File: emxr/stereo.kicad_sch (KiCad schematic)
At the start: 56 parts, among them IC401 NJM2068DD, IC402 NJM4580, IC403 NJM2068DD, IC404 NJM4580

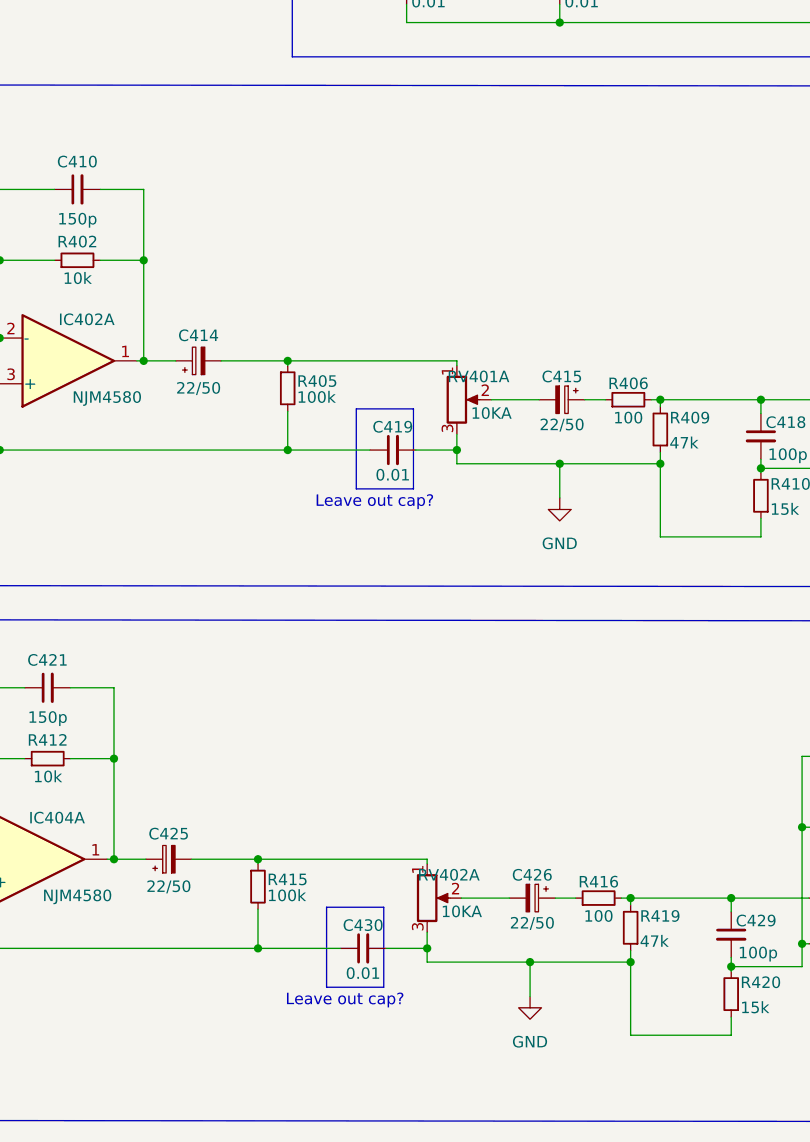
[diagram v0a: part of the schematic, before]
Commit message: finish footprints, starting on component placement
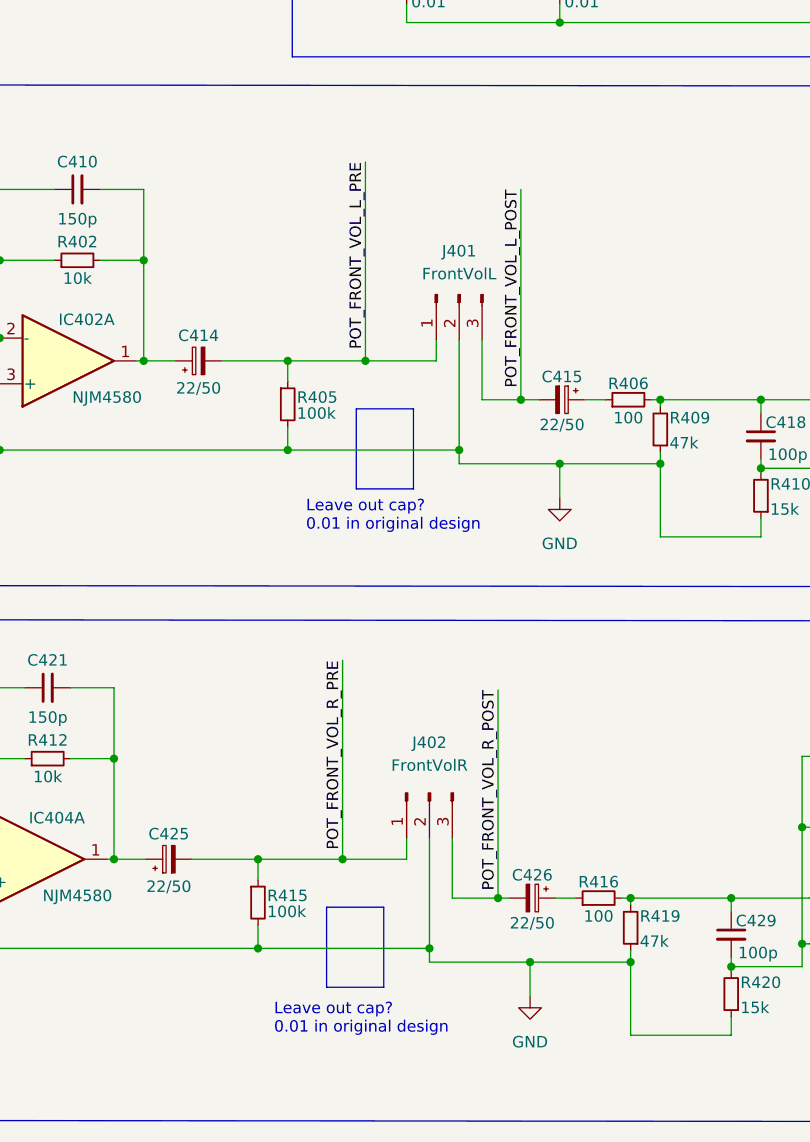
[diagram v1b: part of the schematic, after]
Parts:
- removed C419, C430: 0.01, symbol Device:C_Small
- removed RV401, RV402: 10KA, symbol Device:R_Potentiometer_Dual_Separate
- added J401: FrontVolL, Connector_JST:JST_XH_B3B-XH-A_1x03_P2.50mm_Vertical, symbol Connector:Conn_01x03_Male
- added J402: FrontVolR, Connector_JST:JST_XH_B3B-XH-A_1x03_P2.50mm_Vertical, symbol Connector:Conn_01x03_Male
- C401, C402, C403, C404, C405, C406, C407, C408, C409, C420: footprint (none) -> Capacitor_THT:C_Disc_D3.8mm_W2.6mm_P2.50mm
- C410, C411, C416, C418, C421, C422, C427: footprint (none) -> Capacitor_THT:C_Disc_D5.0mm_W2.5mm_P2.50mm
- C412, C423: footprint (none) -> Capacitor_THT:CP_Radial_D10.0mm_P5.00mm
- C413, C414, C415, C424, C425, C426: footprint (none) -> Capacitor_THT:CP_Radial_D5.0mm_P2.00mm
- C417, C428: footprint (none) -> Capacitor_THT:CP_Radial_D6.3mm_P2.50mm
- C429: footprint (none) -> Capacitor_THT:C_Disc_D5.1mm_W3.2mm_P5.00mm
- IC401, IC402, IC403, IC404: footprint (none) -> Package_DIP:DIP-8_W7.62mm_Socket_LongPads
- R401, R402, R403, R404, R405, R406, R407, R408, R409, R410, R411, R412, R413, R414, R415, R416, R417, R418, R419, R420: footprint (none) -> Resistor_THT:R_Axial_DIN0207_L6.3mm_D2.5mm_P10.16mm_Horizontal
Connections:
- net GND: now also J401.2 (Pin_2), J402.2 (Pin_2)
- net POT_FRONT_VOL_L_PRE: now reaches C414.2, R405.1
- net POT_FRONT_VOL_L_PRE: now also J401.1 (Pin_1)
- net POT_FRONT_VOL_L_POST: now reaches C415.2
- net POT_FRONT_VOL_L_POST: now also J401.3 (Pin_3)
- net POT_FRONT_VOL_R_PRE: now reaches C425.2, R415.1
- net POT_FRONT_VOL_R_PRE: now also J402.1 (Pin_1)
- net POT_FRONT_VOL_R_POST: now reaches C426.2
- net POT_FRONT_VOL_R_POST: now also J402.3 (Pin_3)
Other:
- note added: "Leave out cap? 0.01 in original design"
- note removed: "Leave out cap?"
- moved on the sheet: R405, R415

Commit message: replicated layout
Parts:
- removed C403, C404, C407, C408: 0.01, Capacitor_THT:C_Disc_D3.8mm_W2.6mm_P2.50mm, symbol Device:C_Small
- removed C420: 47p, Capacitor_THT:C_Disc_D3.8mm_W2.6mm_P2.50mm, symbol Device:C_Small
- removed C421, C422: 150p, Capacitor_THT:C_Disc_D5.0mm_W2.5mm_P2.50mm, symbol Device:C_Small
- removed C423: 220/25, Capacitor_THT:CP_Radial_D10.0mm_P5.00mm, symbol Device:C_Polarized_Small
- removed C424, C425, C426: 22/50, Capacitor_THT:CP_Radial_D5.0mm_P2.00mm, symbol Device:C_Polarized_Small
- removed C427: 220p, Capacitor_THT:C_Disc_D5.0mm_W2.5mm_P2.50mm, symbol Device:C_Small
- removed C428: 47/50, Capacitor_THT:CP_Radial_D6.3mm_P2.50mm, symbol Device:C_Polarized_Small
- removed C429: 100p, Capacitor_THT:C_Disc_D5.1mm_W3.2mm_P5.00mm, symbol Device:C_Small
- removed IC403: NJM2068DD, Package_DIP:DIP-8_W7.62mm_Socket_LongPads, symbol Device:Opamp_Dual
- removed IC404: NJM4580, Package_DIP:DIP-8_W7.62mm_Socket_LongPads, symbol Device:Opamp_Dual
- removed J402: FrontVolR, Connector_JST:JST_XH_B3B-XH-A_1x03_P2.50mm_Vertical, symbol Connector:Conn_01x03_Male
- removed R411: 27k, Resistor_THT:R_Axial_DIN0207_L6.3mm_D2.5mm_P10.16mm_Horizontal, symbol Device:R_Small
- removed R412, R414: 10k, Resistor_THT:R_Axial_DIN0207_L6.3mm_D2.5mm_P10.16mm_Horizontal, symbol Device:R_Small
- removed R413: 11k, Resistor_THT:R_Axial_DIN0207_L6.3mm_D2.5mm_P10.16mm_Horizontal, symbol Device:R_Small
- removed R415: 100k, Resistor_THT:R_Axial_DIN0207_L6.3mm_D2.5mm_P10.16mm_Horizontal, symbol Device:R_Small
- removed R416: 100, Resistor_THT:R_Axial_DIN0207_L6.3mm_D2.5mm_P10.16mm_Horizontal, symbol Device:R_Small
- removed R417: 330, Resistor_THT:R_Axial_DIN0207_L6.3mm_D2.5mm_P10.16mm_Horizontal, symbol Device:R_Small
- removed R418: 10, Resistor_THT:R_Axial_DIN0207_L6.3mm_D2.5mm_P10.16mm_Horizontal, symbol Device:R_Small
- removed R419: 47k, Resistor_THT:R_Axial_DIN0207_L6.3mm_D2.5mm_P10.16mm_Horizontal, symbol Device:R_Small
- removed R420: 15k, Resistor_THT:R_Axial_DIN0207_L6.3mm_D2.5mm_P10.16mm_Horizontal, symbol Device:R_Small
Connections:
- net BUS_L renamed SIGNAL_IN
- net SINGAL_L_PRE_GEQ renamed SIGNAL_OUT
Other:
- note removed: "OP-AMP Bypass / R"
- note removed: "STEREO R"

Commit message: more cleaning up/finishing touches
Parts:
- renumbered C405 to C403, C406 to C404, C409 to C405, C410 to C406, C411 to C407, C412 to C408, C413 to C409, C414 to C410, C415 to C411, C416 to C412, C417 to C413, C418 to C414, R406 to R405, R405 to R406
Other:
- moved on the sheet: R403
